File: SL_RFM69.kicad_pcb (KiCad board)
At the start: 4 copper layers, 70 x 51.4 mm, 12 parts, among them SW1 SW_DIP_x08, U1 RFM69HCW

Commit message: Add numbering to DIP
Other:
- board text added: "1"
- board text added: "2"
- board text added: "3"
- board text added: "4"
- board text added: "5"
- board text added: "6"
- board text added: "7"
- board text added: "8"

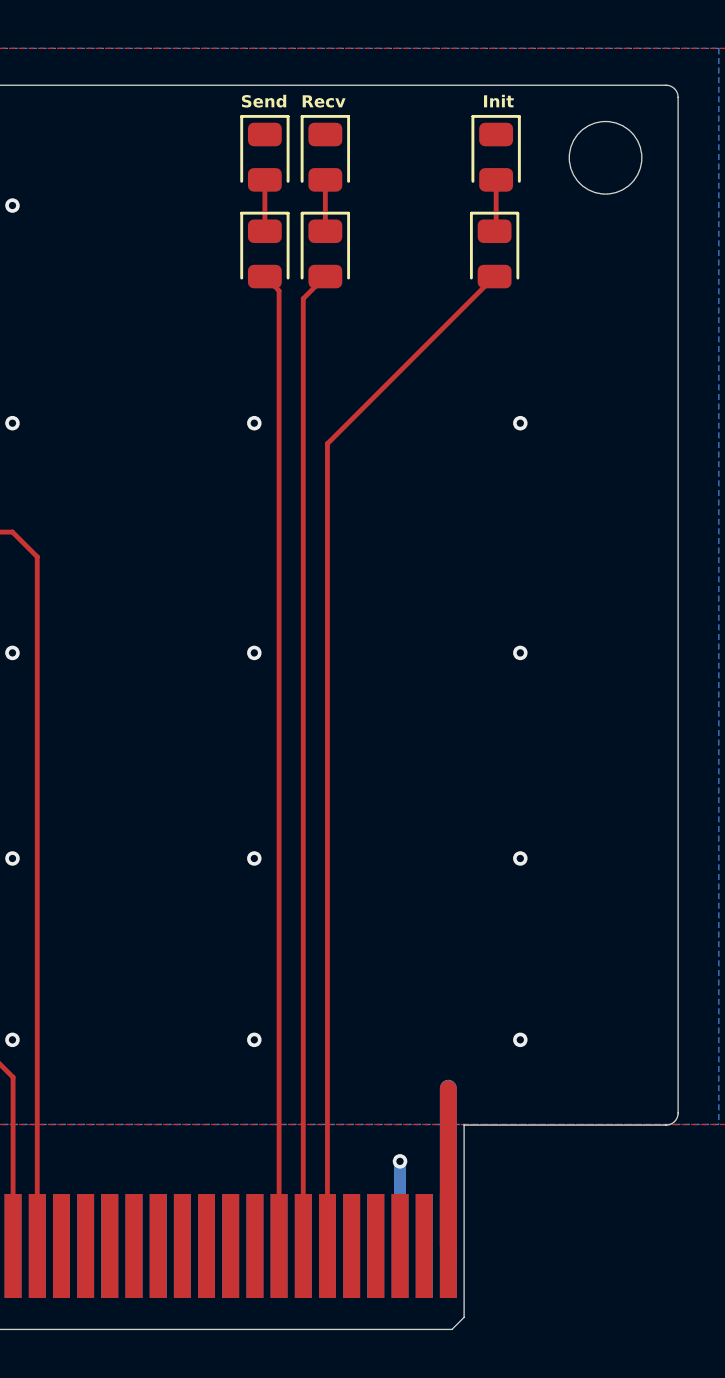
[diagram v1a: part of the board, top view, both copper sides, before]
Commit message: Add power led
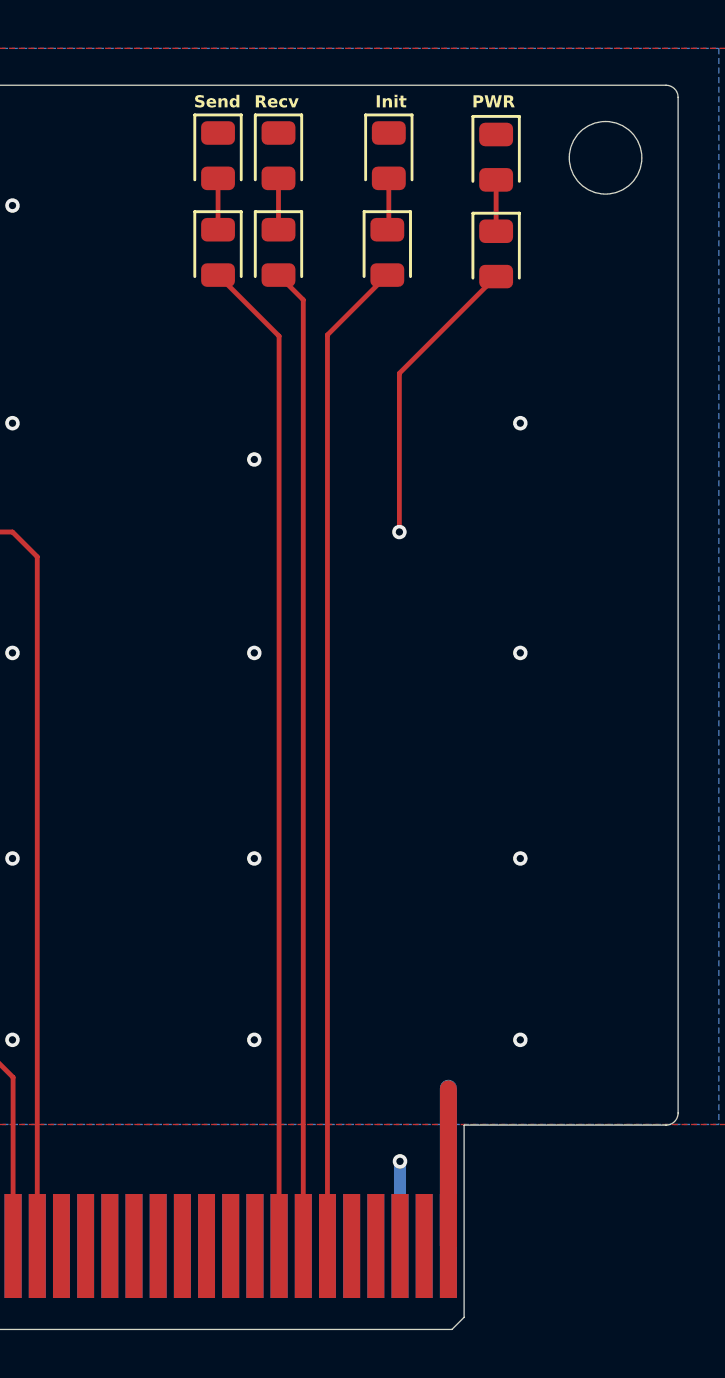
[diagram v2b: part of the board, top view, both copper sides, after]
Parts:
- added D7: Green, LED_SMD:LED_0805_2012Metric, F.Cu at (180.0, 75.0)
- added R4: 470, LED_SMD:LED_0805_2012Metric, F.Cu at (180.0, 79.0)
- D4: value INIT -> Blue
- D5: value RECV -> Orange
- D6: value SEND -> Red
- R1, R2, R3: value 220 -> 470
- moved D4 4.44 mm to (175.6, 74.9)
- moved R1 4.44 mm to (175.5, 78.9)
- moved D5 1.94 mm to (171.0, 74.9)
- moved D6 1.94 mm to (168.5, 74.9)
- moved R2 1.94 mm to (171.0, 78.9)
- moved R3 1.94 mm to (168.5, 78.9)
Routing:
- net +3.3V: track 73.7 -> 87.4 mm, vias 3 -> 4
- net Net-(D7-A): track 0.00 -> 2.12 mm
- net /RFM_INIT: track 43.0 -> 41.2 mm
- net /RFM_SEND: track 40.3 -> 41.2 mm
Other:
- board text added: "PWR"
